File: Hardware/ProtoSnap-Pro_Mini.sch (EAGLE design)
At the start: 59 parts, among them Q1 16MHz, U1 ATMEGA328, U2 MIC5205, U3 FT232RLSSOP, U4 TEMT6000, X2 USB-SMD-NS

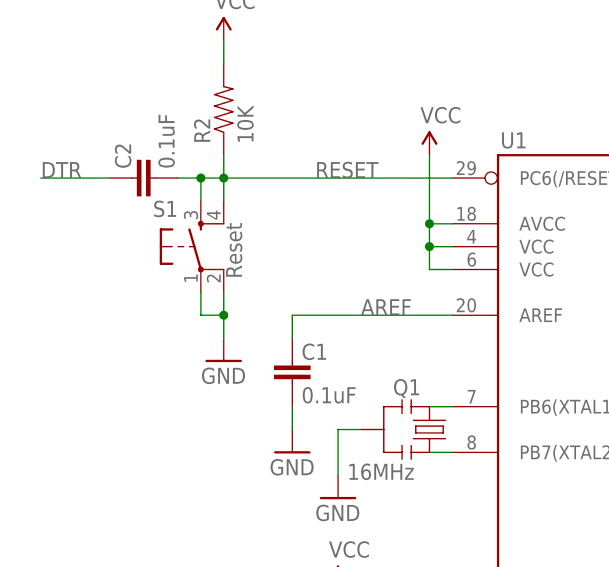
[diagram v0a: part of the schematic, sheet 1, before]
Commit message: Updated packages on resonator, buttons and leds
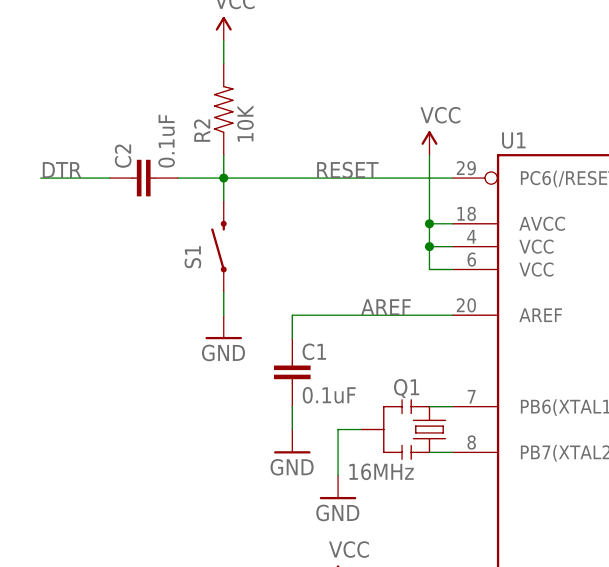
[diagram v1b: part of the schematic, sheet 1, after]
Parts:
- D3, LED1, LED2, LED3: device SparkFun-LED:LEDQC -> Testing:LEDLED-ALT1
- Q1: device SparkFun:RESONATORSMD -> Testing:RESONATOR1:1
- S1: value Reset -> SWITCH-MOMENTARY-2SMD-ALT01; device SparkFun:TAC_SWITCHSMD -> Testing:SWITCH-MOMENTARY-2SMD-ALT01
- S2: value SWITCH-MOMENTARY-2SMD -> SWITCH-MOMENTARY-2SMD-ALT01; device SparkFun:SWITCH-MOMENTARY-2SMD -> Testing:SWITCH-MOMENTARY-2SMD-ALT01
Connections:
- net GND: no longer S1.2
- net RESET: now also S1.2; no longer S1.3, S1.4

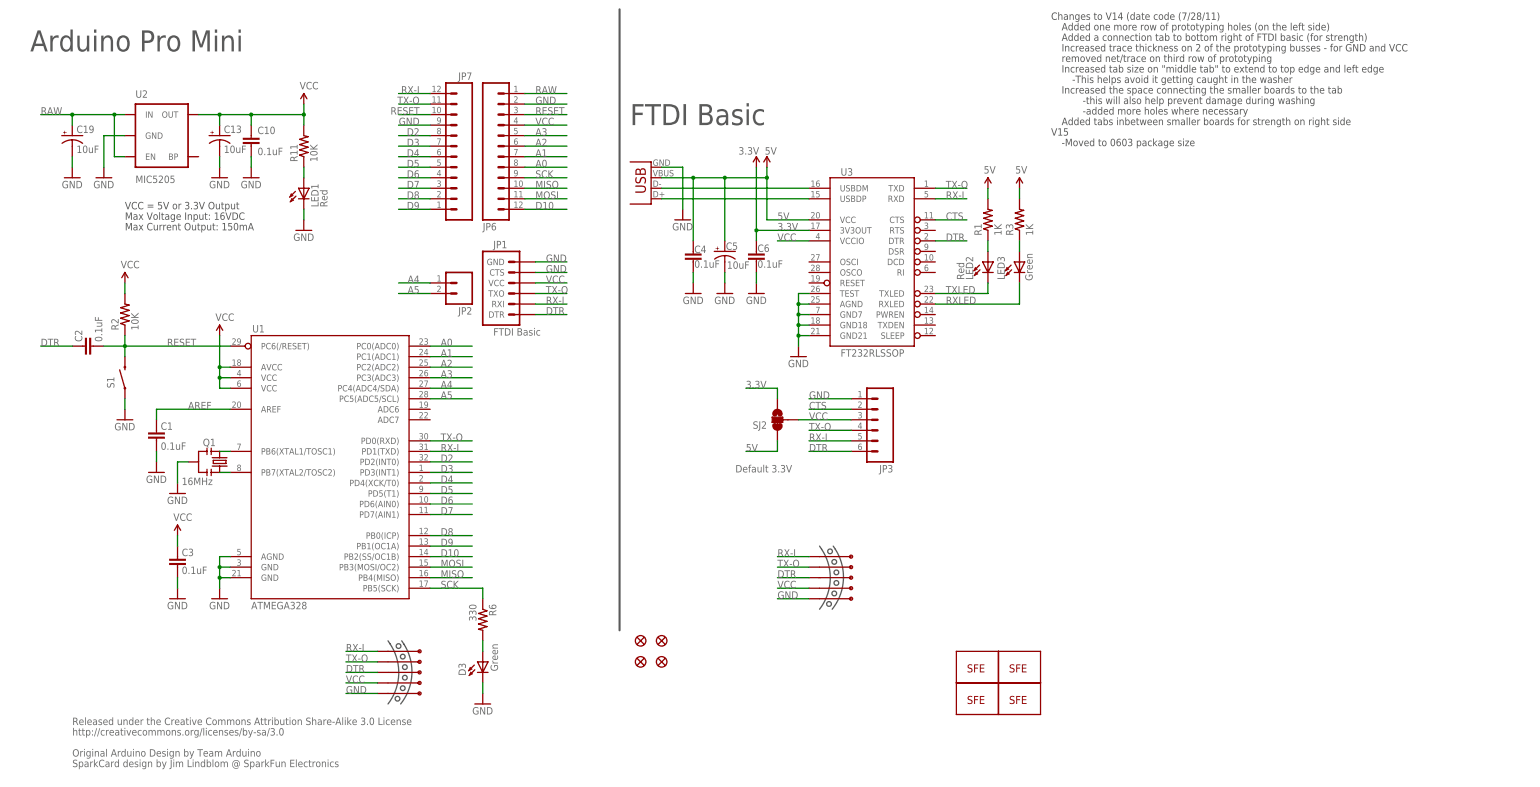
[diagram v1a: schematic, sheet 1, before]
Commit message: Switched to flags in sch, added new frame
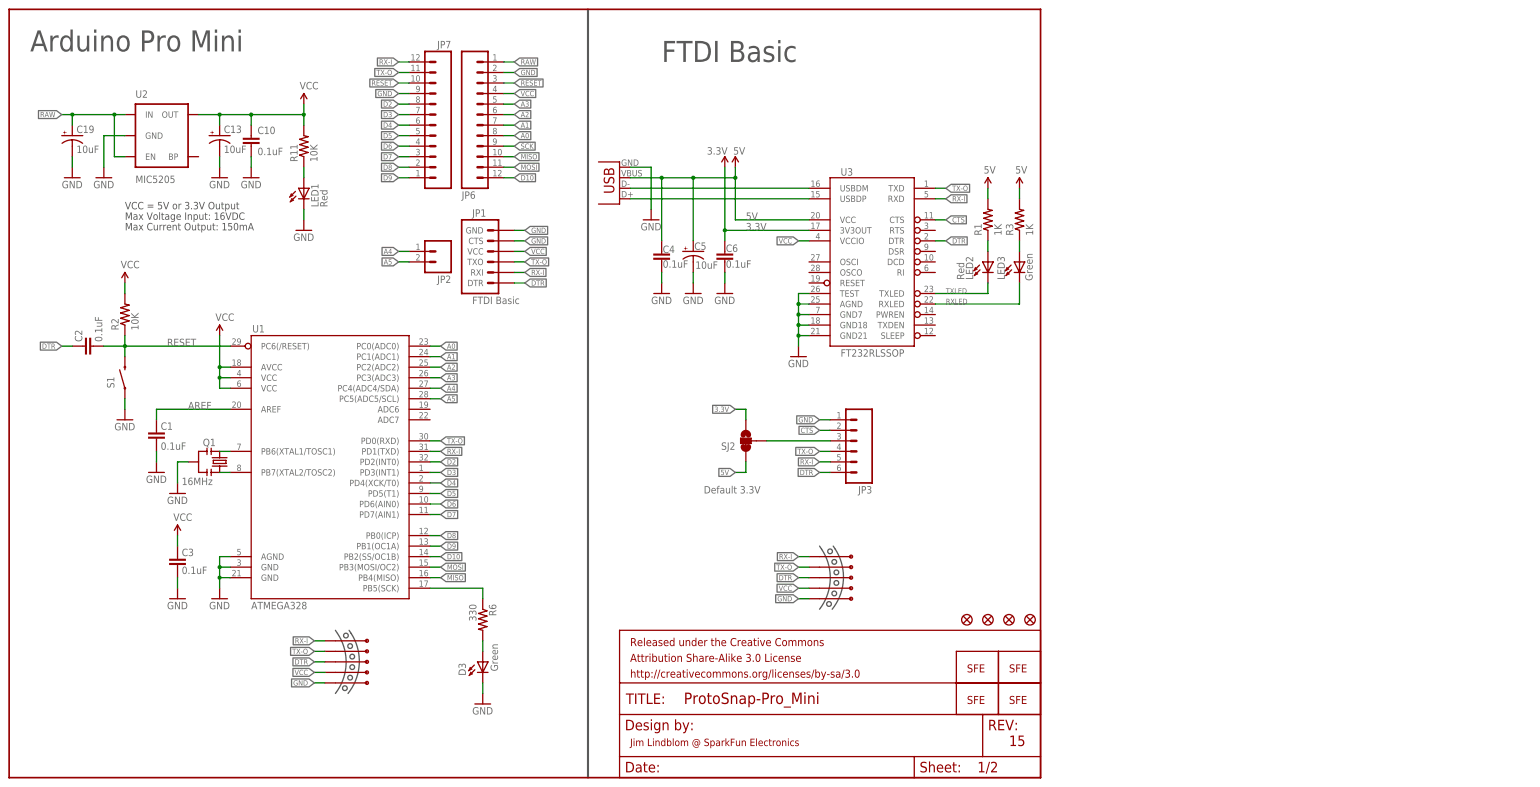
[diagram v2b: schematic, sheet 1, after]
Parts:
- added FRAME1: FRAME-LETTER, SparkFun-Aesthetics:FRAME-LETTER
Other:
- note added: "15"
- note added: "Jim Lindblom @ SparkFun Electronics"
- note removed: "-Moved to 0603 package size"
- note removed: "-This helps avoid it getting caught in the washer"
- note removed: "-added more holes where necessary"
- note removed: "-this will also help prevent damage during washing"
- note removed: "Added a connection tab to bottom right of FTDI basic (for strength)"
- note removed: "Added one more row of prototyping holes (on the left side)"
- note removed: "Added tabs inbetween smaller boards for strength on right side"
- note removed: "Changes to V14 (date code (7/28/11)"
- note removed: "Increased tab size on "middle tab" to extend to top edge and left edge"
- note removed: "Increased the space connecting the smaller boards to the tab"
- note removed: "Increased trace thickness on 2 of the prototyping busses - for GND and VCC"
- note removed: "V15"
- note removed: "removed net/trace on third row of prototyping"
- moved on the sheet: C4, C5, C6, JP1, JP10, JP2, JP21, JP3, JP6, JP7, JP8, JP9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

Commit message: added OSHW logo
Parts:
- added LOGO1: OSHW-LOGOS, SparkFun-Aesthetics:OSHW-LOGOS
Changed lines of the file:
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@@
 <part name="S1" library="Testing" deviceset="SWITCH-MOMENTARY-2" device="SMD-ALT01" value=""/>
 <part name="S2" library="Testing" deviceset="SWITCH-MOMENTARY-2" device="SMD-ALT01" value=""/>
+<part name="LOGO1" library="SparkFun-Aesthetics" deviceset="OSHW-LOGO" device="S"/>
 </parts>
 <sheets>
@@
 <instance part="JP22" gate="G$1" x="246.38" y="38.1"/>
 <instance part="S1" gate="G$1" x="27.94" y="96.52" rot="R90"/>
+<instance part="LOGO1" gate="G$1" x="236.22" y="50.8"/>
 </instances>
 <busses>

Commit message: Switched light sensor to ALS-PT19
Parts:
- removed U4: TEMT6000, SparkFun:TEMT6000
- added U5: ALS-PT19, SparkFun-Sensors:LIGHTSENSORALS
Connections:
- net A0: now also U5.E1; no longer U4.E1
- net VCC: now also U5.C1; no longer U4.C1
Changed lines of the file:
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@@
 <part name="R7" library="SparkFun" deviceset="RESISTOR" device="0603-RES" value="100"/>
 <part name="SG1" library="SparkFun" deviceset="BUZZER" device="SMD2"/>
-<part name="U4" library="SparkFun" deviceset="TEMT6000" device=""/>
 <part name="P+6" library="SparkFun" deviceset="VCC" device=""/>
 <part name="R8" library="SparkFun" deviceset="RESISTOR" device="0603-RES" value="10k"/>
@@
 <part name="S2" library="Testing" deviceset="SWITCH-MOMENTARY-2" device="SMD-ALT01" value=""/>
 <part name="LOGO1" library="SparkFun-Aesthetics" deviceset="OSHW-LOGO" device="S"/>
+<part name="U5" library="SparkFun-Sensors" deviceset="LIGHTSENSOR" device="ALS" value="ALS-PT19"/>
 </parts>
 <sheets>
@@
 <instance part="R7" gate="G$1" x="73.66" y="157.48"/>
 <instance part="SG1" gate="G$1" x="60.96" y="88.9" rot="R270"/>
-<instance part="U4" gate="G$1" x="73.66" y="45.72" smashed="yes" rot="MR0">
-<attribute name="NAME" x="68.58" y="43.18" size="1.778" layer="95" rot="MR90"/>
-<attribute name="VALUE" x="78.74" y="38.1" size="1.778" layer="96" rot="MR90"/>
-</instance>
 <instance part="P+6" gate="1" x="109.22" y="167.64"/>
 <instance part="R8" gate="G$1" x="71.12" y="30.48" rot="MR90"/>
@@
 <instance part="JP21" gate="G$1" x="40.64" y="127"/>
 <instance part="S2" gate="G$1" x="66.04" y="121.92" rot="R270"/>
+<instance part="U5" gate="G$1" x="73.66" y="45.72" smashed="yes" rot="MR0">
+<attribute name="VALUE" x="76.2" y="43.18" size="1.778" layer="96" rot="MR180"/>
+<attribute name="NAME" x="76.2" y="50.8" size="1.778" layer="95" rot="MR180"/>
+</instance>
 </instances>
 <busses>
@@
 <segment>
 <wire x1="71.12" y1="53.34" x2="71.12" y2="50.8" width="0.1524" layer="91"/>
-<pinref part="U4" gate="G$1" pin="C1"/>
 <pinref part="P+7" gate="1" pin="VCC"/>
+<pinref part="U5" gate="G$1" pin="C1"/>
 </segment>
 <segment>
@@
 <wire x1="71.12" y1="38.1" x2="71.12" y2="40.64" width="0.1524" layer="91"/>
 <junction x="71.12" y="38.1"/>
-<pinref part="U4" gate="G$1" pin="E1"/>
 <pinref part="R8" gate="G$1" pin="2"/>
 <pinref part="JP10" gate="G$1" pin="2"/>
 <wire x1="71.12" y1="38.1" x2="48.26" y2="38.1" width="0.1524" layer="91"/>
 <label x="66.04" y="38.1" size="1.27" layer="95"/>
-</segment>
-<segment>
+<pinref part="U5" gate="G$1" pin="E1"/>
+</segment>
+<segment>

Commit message: changed micro fiducials to regular size
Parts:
- removed JP16, JP19, JP20, JP22: FIDUCIAL1X2.5, abes:FIDUCIAL1X2.5
- added FID1, FID2: FIDUCIAL1X2, SparkFun-Aesthetics:FIDUCIAL1X2
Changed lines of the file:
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@@
 <part name="JP18" library="SparkFun" deviceset="LOGO-SFE" device="NEW"/>
 <part name="JP17" library="SparkFun" deviceset="LOGO-SFE" device="SK"/>
-<part name="JP19" library="abes" deviceset="FIDUCIAL" device="1X2.5"/>
-<part name="JP20" library="abes" deviceset="FIDUCIAL" device="1X2.5"/>
-<part name="JP16" library="abes" deviceset="FIDUCIAL" device="1X2.5"/>
-<part name="JP22" library="abes" deviceset="FIDUCIAL" device="1X2.5"/>
 <part name="FRAME2" library="SparkFun" deviceset="FRAME-LETTER" device=""/>
 <part name="LED4" library="SparkFun" deviceset="LED-TRICOLOR" device=""/>
@@
 <part name="LOGO1" library="SparkFun-Aesthetics" deviceset="OSHW-LOGO" device="S"/>
 <part name="U5" library="SparkFun-Sensors" deviceset="LIGHTSENSOR" device="ALS" value="ALS-PT19"/>
+<part name="FID1" library="SparkFun-Aesthetics" deviceset="FIDUCIAL" device="1X2"/>
+<part name="FID2" library="SparkFun-Aesthetics" deviceset="FIDUCIAL" device="1X2"/>
 </parts>
 <sheets>
@@
 <instance part="JP18" gate="G$1" x="241.3" y="25.4"/>
 <instance part="JP17" gate="G$1" x="231.14" y="25.4"/>
-<instance part="JP19" gate="G$1" x="231.14" y="38.1"/>
-<instance part="JP20" gate="G$1" x="236.22" y="38.1"/>
-<instance part="JP16" gate="G$1" x="241.3" y="38.1"/>
-<instance part="JP22" gate="G$1" x="246.38" y="38.1"/>
 <instance part="S1" gate="G$1" x="27.94" y="96.52" rot="R90"/>
 <instance part="LOGO1" gate="G$1" x="236.22" y="50.8"/>
+<instance part="FID1" gate="G$1" x="246.38" y="38.1"/>
+<instance part="FID2" gate="G$1" x="241.3" y="38.1"/>
 </instances>
 <busses>
